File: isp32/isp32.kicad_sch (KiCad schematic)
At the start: 94 parts, among them J1 BAT1, J2 Switching, J3 USB_C_Receptacle_USB2.0, J4 ESP_JTAG, J5 GPS_ANT, J6 F0, J7 F1, J8 Flash_SPI, M1 Motor_Servo, M2 Motor_Servo, M3 Motor_Servo, M4 Motor_Servo, Q1 BSS138, Q2 BSS138, Q3 IRLML6402, Q4 BSS138, Q5 IRLML6402, Q6 S8050, Q7 S8050, Q8 S8050, SW1 RST, SW2 IO0, U10 BMP280, U11 MPU-9250, U12 CH340C, U2 USBLC6-2SC6, U3 ESP32-WROOM-32U, U4 AMS1117-3.3, U5 MP2303ADN, U7 NEO-XM, U8 AT25SF081-SSHD-X, U9 RFM98W-315S2

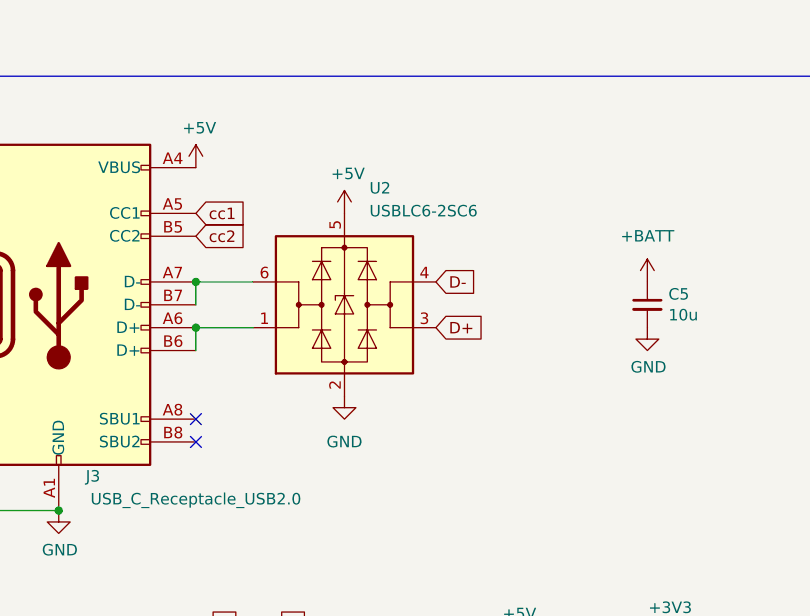
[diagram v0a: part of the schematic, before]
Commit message: Fix ESD
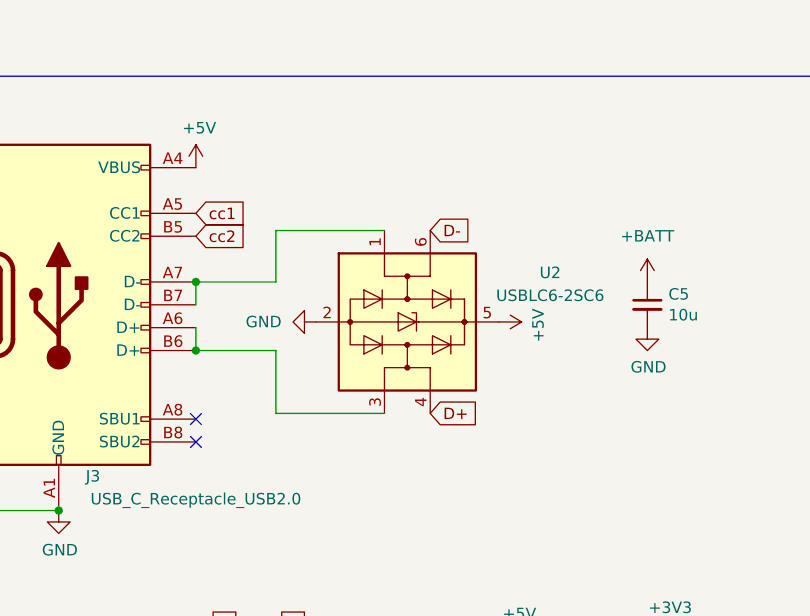
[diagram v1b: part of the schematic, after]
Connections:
- net D+: now also U2.4 (I/O2); no longer U2.3 (I/O2)
- net D-: now also U2.6 (I/O1); no longer U2.4 (I/O2)
- net at J3.A6 (D+), J3.B6 (D+): now also U2.3 (I/O2); no longer U2.1 (I/O1)
- net at J3.A7 (D-), J3.B7 (D-): now also U2.1 (I/O1); no longer U2.6 (I/O1)
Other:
- moved on the sheet: U2
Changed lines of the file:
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@@
   (junction (at 240.665 80.01) (diameter 0) (color 0 0 0 0)
   )
-  (junction (at 60.325 43.18) (diameter 0) (color 0 0 0 0)
-  )
   (junction (at 60.96 146.05) (diameter 0) (color 0 0 0 0)
   )
@@
   (junction (at 314.96 82.55) (diameter 0) (color 0 0 0 0)
   )
-  (junction (at 60.325 48.26) (diameter 0) (color 0 0 0 0)
-  )
   (junction (at 225.425 142.24) (diameter 0) (color 0 0 0 0)
   )
@@
   (junction (at 95.885 89.535) (diameter 0) (color 0 0 0 0)
   )
+  (junction (at 60.325 43.18) (diameter 0) (color 0 0 0 0)
+  )
+  (junction (at 60.325 50.8) (diameter 0) (color 0 0 0 0)
+  )
   (junction (at 240.665 97.79) (diameter 0) (color 0 0 0 0)
   )
@@
     (stroke (width 0) (type default) (color 0 0 0 0))
   )
-  (wire (pts (xy 60.325 43.18) (xy 66.675 43.18))
-    (stroke (width 0) (type default) (color 0 0 0 0))
-  )
   (wire (pts (xy 191.135 46.355) (xy 191.135 51.435))
     (stroke (width 0) (type default) (color 0 0 0 0))
@@
     (stroke (width 0) (type default) (color 0 0 0 0))
   )
-  (wire (pts (xy 60.325 48.26) (xy 66.675 48.26))
-    (stroke (width 0) (type default) (color 0 0 0 0))
-  )
   (wire (pts (xy 88.265 89.535) (xy 95.885 89.535))
     (stroke (width 0) (type default) (color 0 0 0 0))
@@
     (stroke (width 0) (type default) (color 0 0 0 0))
   )
+  (wire (pts (xy 60.325 50.8) (xy 69.215 50.8))
+    (stroke (width 0) (type default) (color 0 0 0 0))
+  )
   (polyline (pts (xy 270.51 71.755) (xy 270.51 104.14))
     (stroke (width 0) (type default) (color 0 0 0 0))
@@
     (stroke (width 0) (type default) (color 0 0 0 0))
   )
+  (wire (pts (xy 69.215 50.8) (xy 69.215 57.785))
+    (stroke (width 0) (type default) (color 0 0 0 0))
+  )
   (wire (pts (xy 345.44 46.99) (xy 345.44 45.085))
     (stroke (width 0) (type default) (color 0 0 0 0))
@@
     (stroke (width 0) (type default) (color 0 0 0 0))
   )
+  (wire (pts (xy 60.325 43.18) (xy 69.215 43.18))
+    (stroke (width 0) (type default) (color 0 0 0 0))
+  )
   (wire (pts (xy 42.545 146.05) (xy 52.07 146.05))
     (stroke (width 0) (type default) (color 0 0 0 0))
@@
     (stroke (width 0) (type default) (color 0 0 0 0))
   )
+  (wire (pts (xy 69.215 57.785) (xy 81.28 57.785))
+    (stroke (width 0) (type default) (color 0 0 0 0))
+  )
   (wire (pts (xy 240.665 97.79) (xy 243.205 97.79))
     (stroke (width 0) (type default) (color 0 0 0 0))
@@
     (stroke (width 0) (type default) (color 0 0 0 0))
   )
+  (wire (pts (xy 69.215 43.18) (xy 69.215 37.465))
+    (stroke (width 0) (type default) (color 0 0 0 0))
+  )
   (wire (pts (xy 52.07 153.67) (xy 52.07 157.48))
     (stroke (width 0) (type default) (color 0 0 0 0))
@@
     (stroke (width 0) (type default) (color 0 0 0 0))
   )
+  (wire (pts (xy 69.215 37.465) (xy 81.28 37.465))
+    (stroke (width 0) (type default) (color 0 0 0 0))
+  )
   (polyline (pts (xy 370.205 146.05) (xy 370.205 199.39))
     (stroke (width 0) (type default) (color 0 0 0 0))
@@
     )
   )
-  (global_label "D-" (shape input) (at 86.995 43.18 0) (fields_autoplaced)
+  (global_label "D-" (shape input) (at 86.36 37.465 0) (fields_autoplaced)
     (effects (font (size 1.27 1.27)) (justify left))
-    (property "Intersheet References" "${INTERSHEET_REFS}" (id 0) (at 92.2505 43.1006 0)
+    (property "Intersheet References" "${INTERSHEET_REFS}" (id 0) (at 91.6155 37.3856 0)
       (effects (font (size 1.27 1.27)) (justify left) hide)
     )
@@
     )
   )
-  (global_label "D+" (shape input) (at 86.995 48.26 0) (fields_autoplaced)
+  (global_label "D+" (shape input) (at 86.36 57.785 0) (fields_autoplaced)
     (effects (font (size 1.27 1.27)) (justify left))
-    (property "Intersheet References" "${INTERSHEET_REFS}" (id 0) (at 92.2505 48.1806 0)
+    (property "Intersheet References" "${INTERSHEET_REFS}" (id 0) (at 91.6155 57.7056 0)
       (effects (font (size 1.27 1.27)) (justify left) hide)
     )
@@
     (pin "2")
   )
-  (symbol (lib_id "power:GND") (at 76.835 55.88 0) (unit 1)
+  (symbol (lib_id "power:GND") (at 73.66 47.625 270) (unit 1)
     (in_bom yes) (on_board yes) (fields_autoplaced)
-    (property "Reference" "#PWR0179" (id 0) (at 76.835 62.23 0)
+    (property "Reference" "#PWR0179" (id 0) (at 67.31 47.625 0)
       (effects (font (size 1.27 1.27)) hide)
     )
-    (property "Value" "GND" (id 1) (at 76.835 60.96 0))
-    (property "Footprint" "" (id 2) (at 76.835 55.88 0)
+    (property "Value" "GND" (id 1) (at 69.85 47.6249 90)
+      (effects (font (size 1.27 1.27)) (justify right))
+    )
+    (property "Footprint" "" (id 2) (at 73.66 47.625 0)
       (effects (font (size 1.27 1.27)) hide)
     )
-    (property "Datasheet" "" (id 3) (at 76.835 55.88 0)
+    (property "Datasheet" "" (id 3) (at 73.66 47.625 0)
       (effects (font (size 1.27 1.27)) hide)
     )
@@
     (pin "1")
   )
-  (symbol (lib_id "Power_Protection:USBLC6-2SC6") (at 76.835 45.72 0) (unit 1)
+  (symbol (lib_id "Power_Protection:USBLC6-2SC6") (at 83.82 47.625 270) (unit 1)
     (in_bom yes) (on_board yes) (fields_autoplaced)
-    (property "Reference" "U2" (id 0) (at 79.6037 32.766 0)
-      (effects (font (size 1.27 1.27)) (justify left))
-    )
-    (property "Value" "USBLC6-2SC6" (id 1) (at 79.6037 35.306 0)
-      (effects (font (size 1.27 1.27)) (justify left))
-    )
-    (property "Footprint" "Package_TO_SOT_SMD:SOT-23-6" (id 2) (at 76.835 58.42 0)
+    (property "Reference" "U2" (id 0) (at 99.695 42.1638 90))
+    (property "Value" "USBLC6-2SC6" (id 1) (at 99.695 44.7038 90))
+    (property "Footprint" "Package_TO_SOT_SMD:SOT-23-6" (id 2) (at 71.12 47.625 0)
       (effects (font (size 1.27 1.27)) hide)
     )
-    (property "Datasheet" "https://www.st.com/resource/en/datasheet/usblc6-2.pdf" (id 3) (at 81.915 36.83 0)
+    (property "Datasheet" "https://www.st.com/resource/en/datasheet/usblc6-2.pdf" (id 3) (at 92.71 52.705 0)
       (effects (font (size 1.27 1.27)) hide)
     )
@@
     (pin "2")
   )
-  (symbol (lib_id "power:+5V") (at 76.835 35.56 0) (unit 1)
+  (symbol (lib_id "power:+5V") (at 93.98 47.625 270) (unit 1)
     (in_bom yes) (on_board yes)
-    (property "Reference" "#PWR0175" (id 0) (at 76.835 39.37 0)
+    (property "Reference" "#PWR0175" (id 0) (at 90.17 47.625 0)
       (effects (font (size 1.27 1.27)) hide)
     )
-    (property "Value" "+5V" (id 1) (at 77.216 31.1658 0))
-    (property "Footprint" "" (id 2) (at 76.835 35.56 0)
+    (property "Value" "+5V" (id 1) (at 98.3742 48.006 0))
+    (property "Footprint" "" (id 2) (at 93.98 47.625 0)
       (effects (font (size 1.27 1.27)) hide)
     )
-    (property "Datasheet" "" (id 3) (at 76.835 35.56 0)
+    (property "Datasheet" "" (id 3) (at 93.98 47.625 0)
       (effects (font (size 1.27 1.27)) hide)
     )

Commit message: Add M3 mounting hole
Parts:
- added H1, H2, H3, H4: MountingHole, MountingHole:MountingHole_3.2mm_M3_ISO7380, symbol Mechanical:MountingHole
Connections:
- net EXT_INT: now also U3.4 (SENSOR_VP)
- no-connect marks 39 -> 38
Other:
- note added: "M3 Mounting Hole"
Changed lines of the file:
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@@
   (no_connect (at 85.725 156.845))
   (no_connect (at 424.815 48.895))
-  (no_connect (at 85.725 128.905))
   (no_connect (at 85.725 131.445))
   (no_connect (at 424.815 46.355))
@@
     (stroke (width 0) (type default) (color 0 0 0 0))
   )
+  (polyline (pts (xy 471.17 109.22) (xy 433.07 109.22))
+    (stroke (width 0) (type default) (color 0 0 0 0))
+  )
   (wire (pts (xy 294.005 82.55) (xy 294.005 80.01))
     (stroke (width 0) (type default) (color 0 0 0 0))
@@
     (stroke (width 0) (type default) (color 0 0 0 0))
   )
+  (polyline (pts (xy 433.07 140.97) (xy 471.17 140.97))
+    (stroke (width 0) (type default) (color 0 0 0 0))
+  )
   (wire (pts (xy 350.52 53.34) (xy 350.52 59.055))
     (stroke (width 0) (type default) (color 0 0 0 0))
@@
     (stroke (width 0) (type default) (color 0 0 0 0))
   )
+  (polyline (pts (xy 433.07 109.22) (xy 433.07 140.97))
+    (stroke (width 0) (type default) (color 0 0 0 0))
+  )
   (polyline (pts (xy 135.255 109.22) (xy 270.51 109.22))
     (stroke (width 0) (type default) (color 0 0 0 0))
@@
     (stroke (width 0) (type default) (color 0 0 0 0))
   )
+  (polyline (pts (xy 471.17 140.97) (xy 471.17 109.22))
+    (stroke (width 0) (type default) (color 0 0 0 0))
+  )
   (wire (pts (xy 60.325 48.26) (xy 60.325 50.8))
     (stroke (width 0) (type default) (color 0 0 0 0))
@@
     (effects (font (size 1.27 1.27)) (justify left bottom))
   )
+  (text "M3 Mounting Hole" (at 435.61 112.395 0)
+    (effects (font (size 1.27 1.27)) (justify left bottom))
+  )
   (text "Servo Motors" (at 372.745 74.295 0)
     (effects (font (size 1.27 1.27)) (justify left bottom))
@@
     )
   )
+  (global_label "EXT_INT" (shape input) (at 85.725 128.905 180) (fields_autoplaced)
+    (effects (font (size 1.27 1.27)) (justify right))
+    (property "Intersheet References" "${INTERSHEET_REFS}" (id 0) (at 76.1152 128.9844 0)
+      (effects (font (size 1.27 1.27)) (justify right) hide)
+    )
+  )
   (global_label "TDO" (shape input) (at 386.08 132.08 0) (fields_autoplaced)
     (effects (font (size 1.27 1.27)) (justify left))
@@
     (pin "1")
   )
+  (symbol (lib_id "Mechanical:MountingHole") (at 446.405 123.19 0) (unit 1)
+    (in_bom yes) (on_board yes) (fields_autoplaced)
+    (property "Reference" "H2" (id 0) (at 448.945 121.9199 0)
+      (effects (font (size 1.27 1.27)) (justify left))
+    )
+    (property "Value" "MountingHole" (id 1) (at 448.945 124.4599 0)
+      (effects (font (size 1.27 1.27)) (justify left))
+    )
+    (property "Footprint" "MountingHole:MountingHole_3.2mm_M3_ISO7380" (id 2) (at 446.405 123.19 0)
+      (effects (font (size 1.27 1.27)) hide)
+    )
+    (property "Datasheet" "~" (id 3) (at 446.405 123.19 0)
+      (effects (font (size 1.27 1.27)) hide)
+    )
+  )
   (symbol (lib_id "RF_Module:RFM98W-315S2") (at 240.665 43.18 0) (unit 1)
     (in_bom yes) (on_board yes)
@@
     (pin "1")
   )
+  (symbol (lib_id "Mechanical:MountingHole") (at 446.405 116.84 0) (unit 1)
+    (in_bom yes) (on_board yes) (fields_autoplaced)
+    (property "Reference" "H1" (id 0) (at 448.945 115.5699 0)
+      (effects (font (size 1.27 1.27)) (justify left))
+    )
+    (property "Value" "MountingHole" (id 1) (at 448.945 118.1099 0)
+      (effects (font (size 1.27 1.27)) (justify left))
+    )
+    (property "Footprint" "MountingHole:MountingHole_3.2mm_M3_ISO7380" (id 2) (at 446.405 116.84 0)
+      (effects (font (size 1.27 1.27)) hide)
+    )
+    (property "Datasheet" "~" (id 3) (at 446.405 116.84 0)
+      (effects (font (size 1.27 1.27)) hide)
+    )
+  )
   (symbol (lib_id "Transistor_BJT:S8050") (at 353.06 90.805 0) (unit 1)
     (in_bom yes) (on_board yes)
@@
     (pin "2")
   )
+  (symbol (lib_id "Mechanical:MountingHole") (at 446.405 130.175 0) (unit 1)
+    (in_bom yes) (on_board yes) (fields_autoplaced)
+    (property "Reference" "H3" (id 0) (at 448.945 128.9049 0)
+      (effects (font (size 1.27 1.27)) (justify left))
+    )
+    (property "Value" "MountingHole" (id 1) (at 448.945 131.4449 0)
+      (effects (font (size 1.27 1.27)) (justify left))
+    )
+    (property "Footprint" "MountingHole:MountingHole_3.2mm_M3_ISO7380" (id 2) (at 446.405 130.175 0)
+      (effects (font (size 1.27 1.27)) hide)
+    )
+    (property "Datasheet" "~" (id 3) (at 446.405 130.175 0)
+      (effects (font (size 1.27 1.27)) hide)
+    )
+  )
   (symbol (lib_id "power:+3V3") (at 328.295 133.35 0) (unit 1)
     (in_bom yes) (on_board yes) (fields_autoplaced)
@@
     (pin "1")
   )
+  (symbol (lib_id "Mechanical:MountingHole") (at 446.405 136.525 0) (unit 1)
+    (in_bom yes) (on_board yes) (fields_autoplaced)
+    (property "Reference" "H4" (id 0) (at 448.945 135.2549 0)
+      (effects (font (size 1.27 1.27)) (justify left))
+    )
+    (property "Value" "MountingHole" (id 1) (at 448.945 137.7949 0)
+      (effects (font (size 1.27 1.27)) (justify left))
+    )
+    (property "Footprint" "MountingHole:MountingHole_3.2mm_M3_ISO7380" (id 2) (at 446.405 136.525 0)
+      (effects (font (size 1.27 1.27)) hide)
+    )
+    (property "Datasheet" "~" (id 3) (at 446.405 136.525 0)
+      (effects (font (size 1.27 1.27)) hide)
+    )
+  )
   (symbol (lib_id "power:+3V3") (at 301.625 140.335 0) (unit 1)
     (in_bom yes) (on_board yes) (fields_autoplaced)
@@
       (reference "D5") (unit 1) (value "POWER") (footprint "LED_SMD:LED_0603_1608Metric")
     )
+    (path "/d742f211-b1a7-47b2-89c7-cb7304182dd9"
+      (reference "H1") (unit 1) (value "MountingHole") (footprint "MountingHole:MountingHole_3.2mm_M3_ISO7380")
+    )
+    (path "/183df840-74bf-486a-8ecd-0847f1a21950"
+      (reference "H2") (unit 1) (value "MountingHole") (footprint "MountingHole:MountingHole_3.2mm_M3_ISO7380")
+    )
+    (path "/da76e172-05f9-4466-8aba-e1657092c231"
+      (reference "H3") (unit 1) (value "MountingHole") (footprint "MountingHole:MountingHole_3.2mm_M3_ISO7380")
+    )
+    (path "/e4f6a6aa-2170-433f-97d5-3335f6f7a296"
+      (reference "H4") (unit 1) (value "MountingHole") (footprint "MountingHole:MountingHole_3.2mm_M3_ISO7380")
+    )
     (path "/b295a68d-dfa6-45c7-b8e0-9f9b289cb4eb"

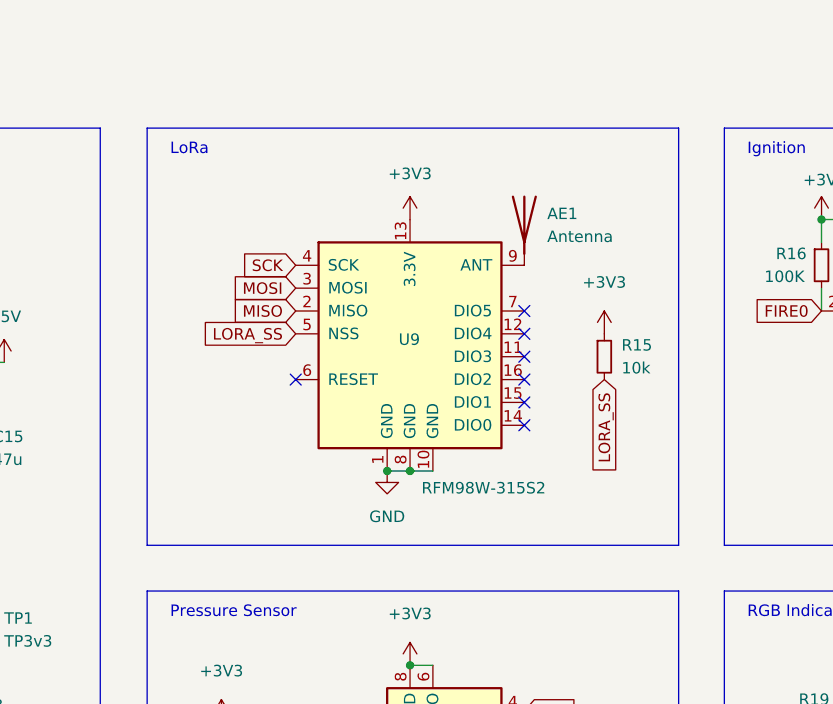
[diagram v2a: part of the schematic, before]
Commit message: Change LoRa antenna
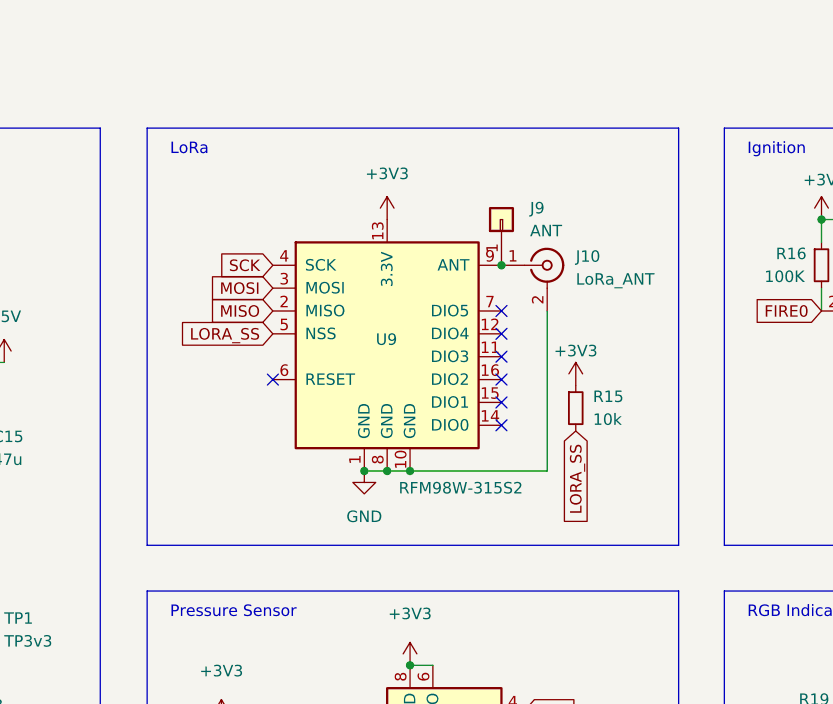
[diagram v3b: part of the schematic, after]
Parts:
- removed AE1: Antenna, Connector_PinHeader_2.00mm:PinHeader_1x01_P2.00mm_Vertical, symbol Device:Antenna
- added J10: LoRa_ANT, Connector_Coaxial:U.FL_Hirose_U.FL-R-SMT-1_Vertical, symbol Connector:Conn_Coaxial
- added J9: ANT, Connector_PinHeader_2.00mm:PinHeader_1x01_P2.00mm_Vertical, symbol Connector_Generic:Conn_01x01
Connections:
- net GND: now also J10.2 (Ext)
- net at U9.9 (ANT): now also J10.1 (In), J9.1 (Pin_1)
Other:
- moved on the sheet: R15, U9
